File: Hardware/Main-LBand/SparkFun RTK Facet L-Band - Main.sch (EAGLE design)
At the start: 123 parts, among them J1 QWIIC_RIGHT_ANGLE, J10 FPC_12_0.5MM_BACKFLIP, J15 FPC_12_0.5MM_BACKFLIP, J18 FPC_12_0.5MM_BACKFLIP, J2 U.FL, J8 FPC_12_0.5MM_BACKFLIP, J9 CORTEX_JTAG_DEBUG_PTH, Q2 MBT3904DW1T1, Q3 SIL2308, U1 74HC4052D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

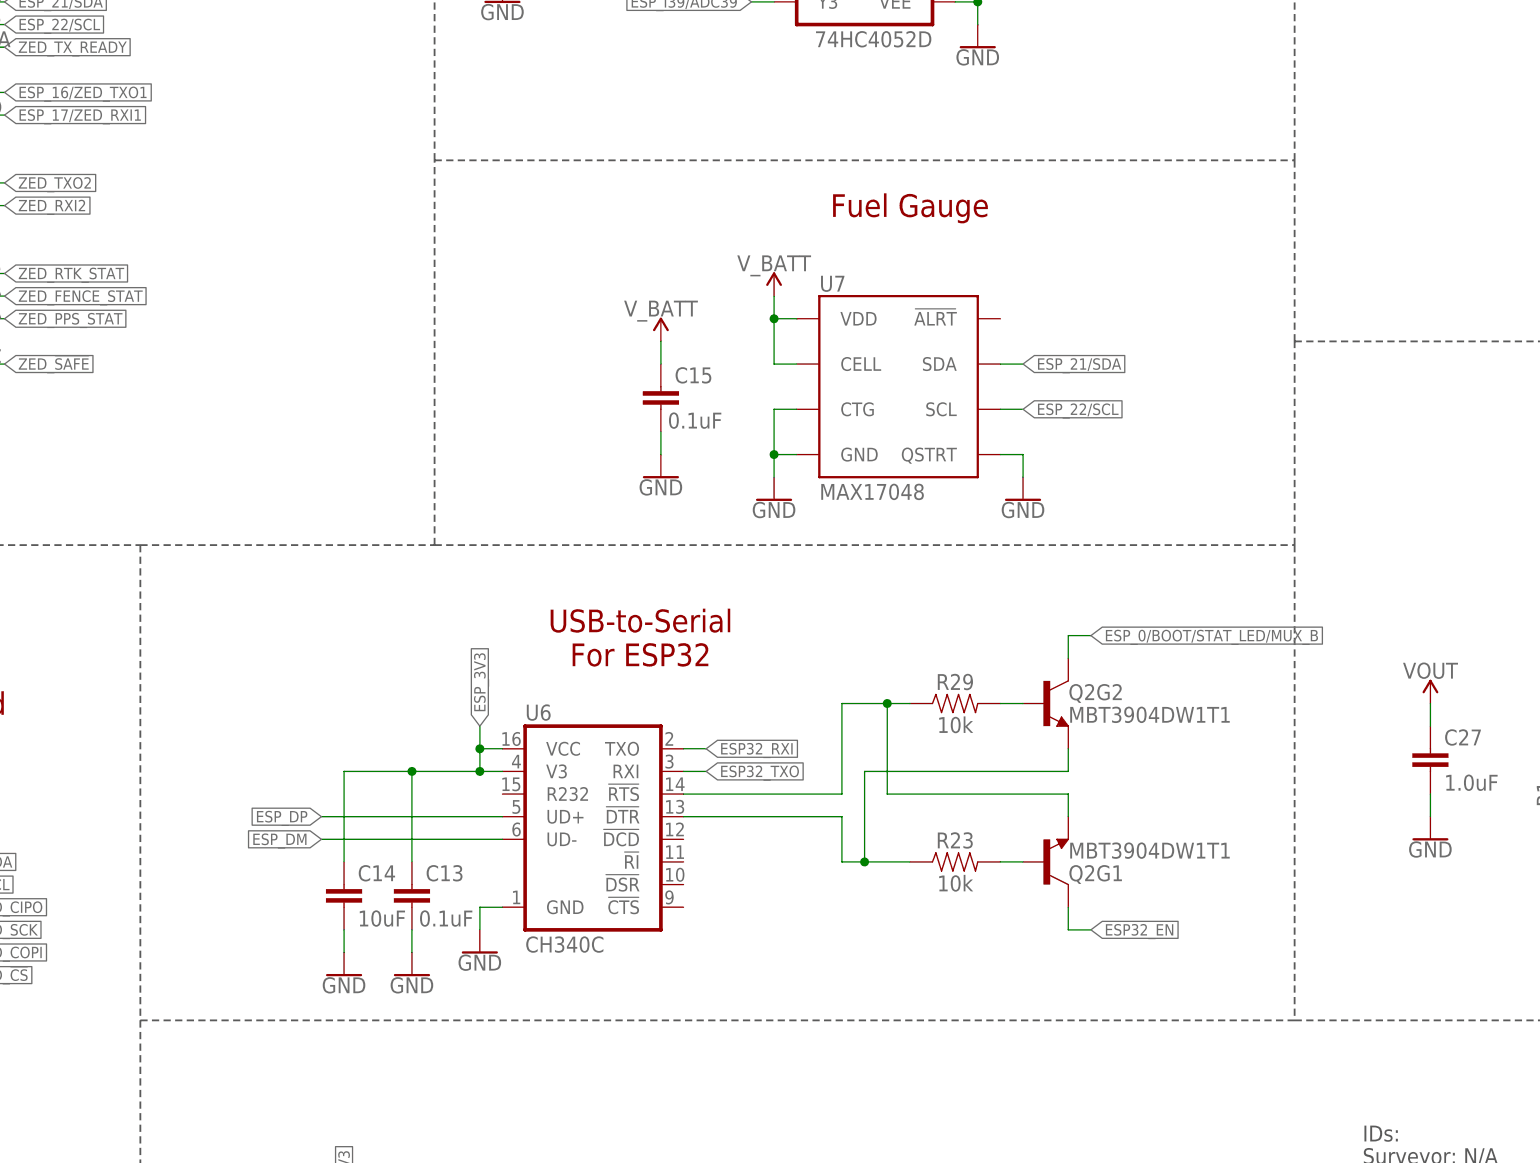
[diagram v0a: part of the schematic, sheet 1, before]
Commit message: Add I2C addresses to schematics
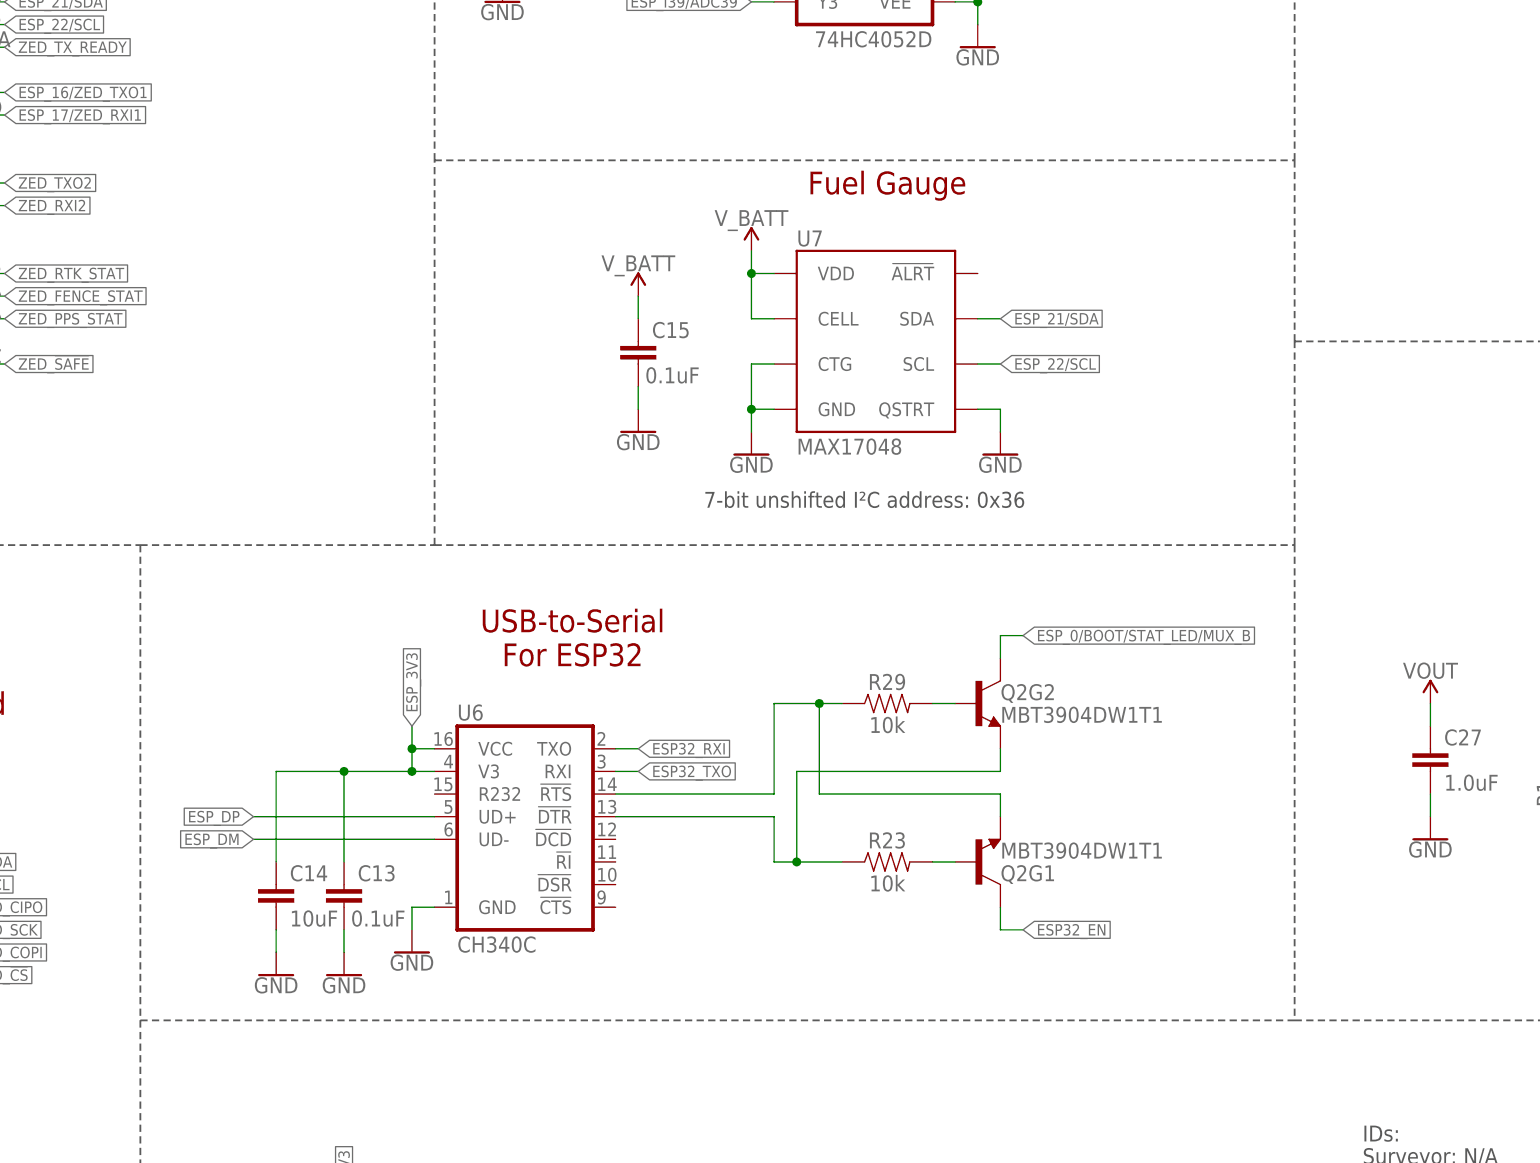
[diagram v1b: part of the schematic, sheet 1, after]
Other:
- note added: "7-bit unshifted I²C address: 0x36"
- moved on the sheet: C13, C14, C15, Q2G1, Q2G2, R23, R29, U6, U7

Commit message: Remove R1, change charger FP, change 33 discretes, ESP32 DFM paste.
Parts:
- added R14, R15, R45, R46, R47, R48, R49, R50: 33, SparkFun-Resistors:33OHM-0603-1/10W-1%
- R1: value DNP -> 33; device SparkFun-Resistors:DNP-0603 -> SparkFun-Resistors:33OHM-0603-1/10W-1%
- R2, R4, R9: device SparkFun-Resistors:33OHM_RA-1206-1/16W-5% -> SparkFun-Resistors:33OHM-0603-1/10W-1%
- R33: value 20k -> 33k; device SparkFun-Resistors:20KOHM-0603-1/10W-1% -> SparkFun-Resistors:33KOHM-0603-1/10W-1%
- U10: value MCP73833 -> MCP73833MSOP; device SparkFun-IC-Power:MCP73833 -> SparkFun-IC-Power:MCP73833MSOP
- U12, U2: value SPX3819M5_3_3 -> AP2112K-3.3V; device SparkFun-IC-Power:V_REG_SPX3819-SOT23-5 -> SparkFun-IC-Power:V_REG_AP2112K-3.3V
- U4: value SPX3819M5_3_3 -> STLQ015-3.3V; device SparkFun-IC-Power:V_REG_SPX3819-SOT23-5 -> SparkFun-IC-Power:STLQ015-3.3V
- U5: value ESP-WROOM-3232D -> ESP-WROOM-3232D-DFMP; device SparkFun-RF:ESP-WROOM-3232D -> SparkFun-RF:ESP-WROOM-3232D-DFMP
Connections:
- net ESP_14/PERIPHERAL_POWER/MTMS: no longer R1.2
- net ESP_17/ZED_RXI1: now also R15.2; no longer R9D.2
- net ESP_21/SDA: now also R4.2; no longer R9C.2
- net ESP_22/SCL: now also R9.2; no longer R9B.2
- net FENCE_LV: now also R48.1; no longer R4A.2
- net GND: no longer R1.1
- net N$16: now also R1.1; no longer R2D.1
- net N$18: now also R50.1; no longer R2C.1
- net N$22: now also R14.1; no longer R9A.1
- net N$5: now also R2.1; no longer R2B.1
- net PPS: now also R49.1; no longer R2A.1
- net RTK_LV: now also R47.1; no longer R4B.2
- net RX2_LV: now also R46.1; no longer R4C.2
- net RXLV: now also R15.1; no longer R9D.1
- net SCL_LV: now also R9.1; no longer R9B.1
- net SDA_LV: now also R4.1; no longer R9C.1
- net TX2_LV: now also R45.1; no longer R4D.2
- net ZED_!RESET!: now also R1.2; no longer R2D.2
- net ZED_!SAFE!: now also R50.2; no longer R2C.2
- net ZED_EXTINT: now also R2.2; no longer R2B.2
- net ZED_FENCE_STAT: now also R48.2; no longer R4A.1
- net ZED_PPS_STAT: now also R49.2; no longer R2A.2
- net ZED_RTK_STAT: now also R47.2; no longer R4B.1
- net ZED_RXI2: now also R46.2; no longer R4C.1
- net ZED_TXO2: now also R45.2; no longer R4D.1
- net ZED_TX_READY: now also R14.2; no longer R9A.2
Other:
- note added: "Facet LBand v14: 10/33"
- moved on the sheet: R1

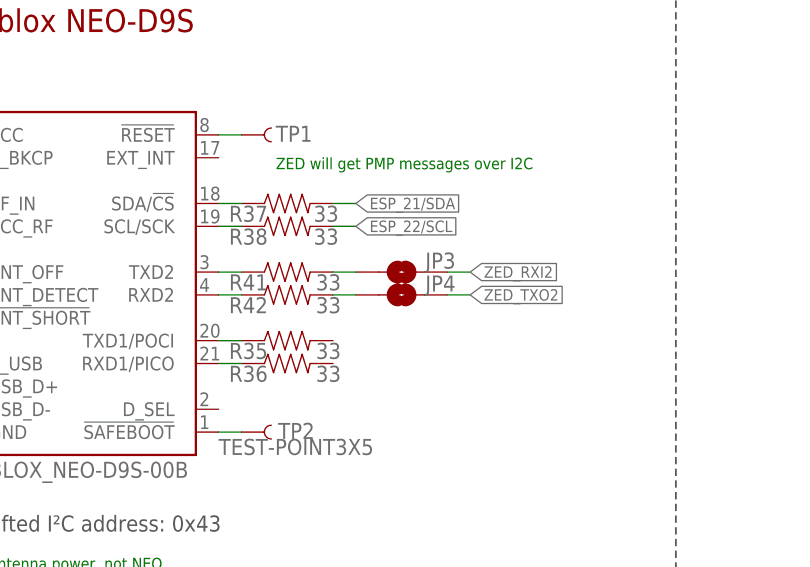
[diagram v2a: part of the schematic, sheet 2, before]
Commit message: Close jumpers between ZED/NEO. Change resistor IDs to indicate L-Band Direct.
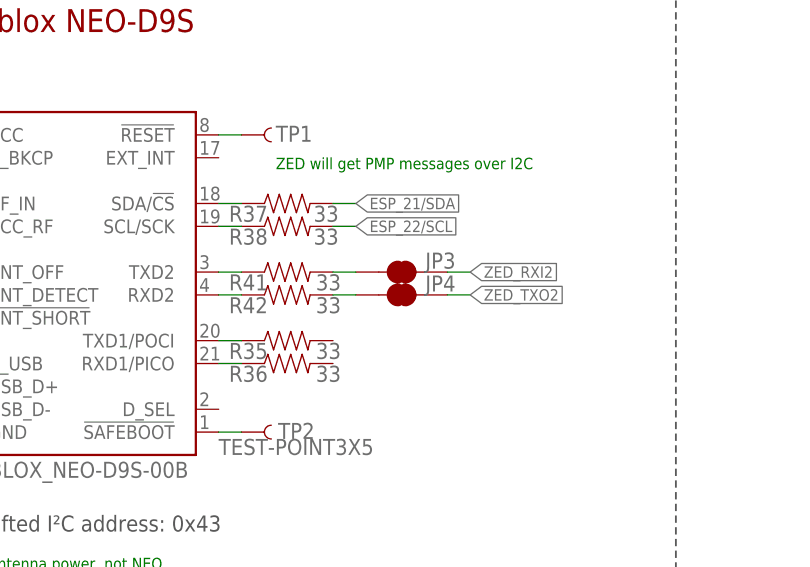
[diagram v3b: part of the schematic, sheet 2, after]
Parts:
- JP3, JP4: value JUMPER-SMT_2_NO_SILK -> JUMPER-SMT_2_NC_TRACE_SILK; device SparkFun-Jumpers:JUMPER-SMT_2_NO_SILK -> SparkFun-Jumpers:JUMPER-SMT_2_NC_TRACE_SILK
- R33: value 33k -> 100k; device SparkFun-Resistors:33KOHM-0603-1/10W-1% -> SparkFun-Resistors:100KOHM-0603-1/10W-1%
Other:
- note added: "Facet LBand Direct: 10/100"
- note added: "Reference Station: 20/10"
- note removed: "Facet LBand v14: 10/33"
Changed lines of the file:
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@@
 <part name="J9" library="SparkFun-Connectors" deviceset="CORTEX_JTAG_DEBUG" device="_PTH"/>
 <part name="GND17" library="SparkFun-PowerSymbols" deviceset="GND" device=""/>
-<part name="R33" library="SparkFun-Resistors" deviceset="33KOHM" device="-0603-1/10W-1%" value="33k"/>
+<part name="R33" library="SparkFun-Resistors" deviceset="100KOHM" device="-0603-1/10W-1%" value="100k"/>
 <part name="R34" library="SparkFun-Resistors" deviceset="10KOHM" device="-0603-1/10W-1%" value="10k"/>
 <part name="GND26" library="SparkFun-PowerSymbols" deviceset="GND" device=""/>
@@
 <part name="J2" library="SparkFun-Connectors" deviceset="U.FL2PIN" device="" value="U.FL"/>
 <part name="R43" library="SparkFun-Resistors" deviceset="100OHM" device="-0603-1/10W-1%" value="100"/>
-<part name="JP3" library="SparkFun-Jumpers" deviceset="JUMPER-SMT_2_NO" device="_SILK" package3d_urn="urn:adsk.eagle:package:39279/1" value=""/>
-<part name="JP4" library="SparkFun-Jumpers" deviceset="JUMPER-SMT_2_NO" device="_SILK" package3d_urn="urn:adsk.eagle:package:39279/1" value=""/>
+<part name="JP3" library="SparkFun-Jumpers" deviceset="JUMPER-SMT_2_NC_TRACE" device="_SILK" package3d_urn="urn:adsk.eagle:package:39281/1" value=""/>
+<part name="JP4" library="SparkFun-Jumpers" deviceset="JUMPER-SMT_2_NC_TRACE" device="_SILK" package3d_urn="urn:adsk.eagle:package:39281/1" value=""/>
 <part name="R1" library="SparkFun-Resistors" deviceset="33OHM" device="-0603-1/10W-1%" value="33"/>
 <part name="R2" library="SparkFun-Resistors" deviceset="33OHM" device="-0603-1/10W-1%" value="33"/>
@@
 <text x="276.86" y="101.6" size="1.778" layer="97" align="center-left">Facet LBand: 10/20</text>
 <text x="220.98" y="185.42" size="1.778" layer="97" align="center">7-bit unshifted I²C address: 0x36</text>
-<text x="276.86" y="99.06" size="1.778" layer="97" align="center-left">Facet LBand v14: 10/33</text>
+<text x="276.86" y="99.06" size="1.778" layer="97" align="center-left">Facet LBand Direct: 10/100</text>
+<text x="276.86" y="96.52" size="1.778" layer="97" align="center-left">Reference Station: 20/10</text>
 </plain>
 <instances>
